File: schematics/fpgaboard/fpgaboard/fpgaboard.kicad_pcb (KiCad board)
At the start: 4 copper layers, 67.6 x 37.5 mm, 14 parts, among them J1 SODIMM-200, U1 LFE5UM-85F-8BG381I, U13 W25Q32JVSS, U2 AMS1117-3.3, U3 IS42S16320F-7TL, U4 IS42S16320F-7TL

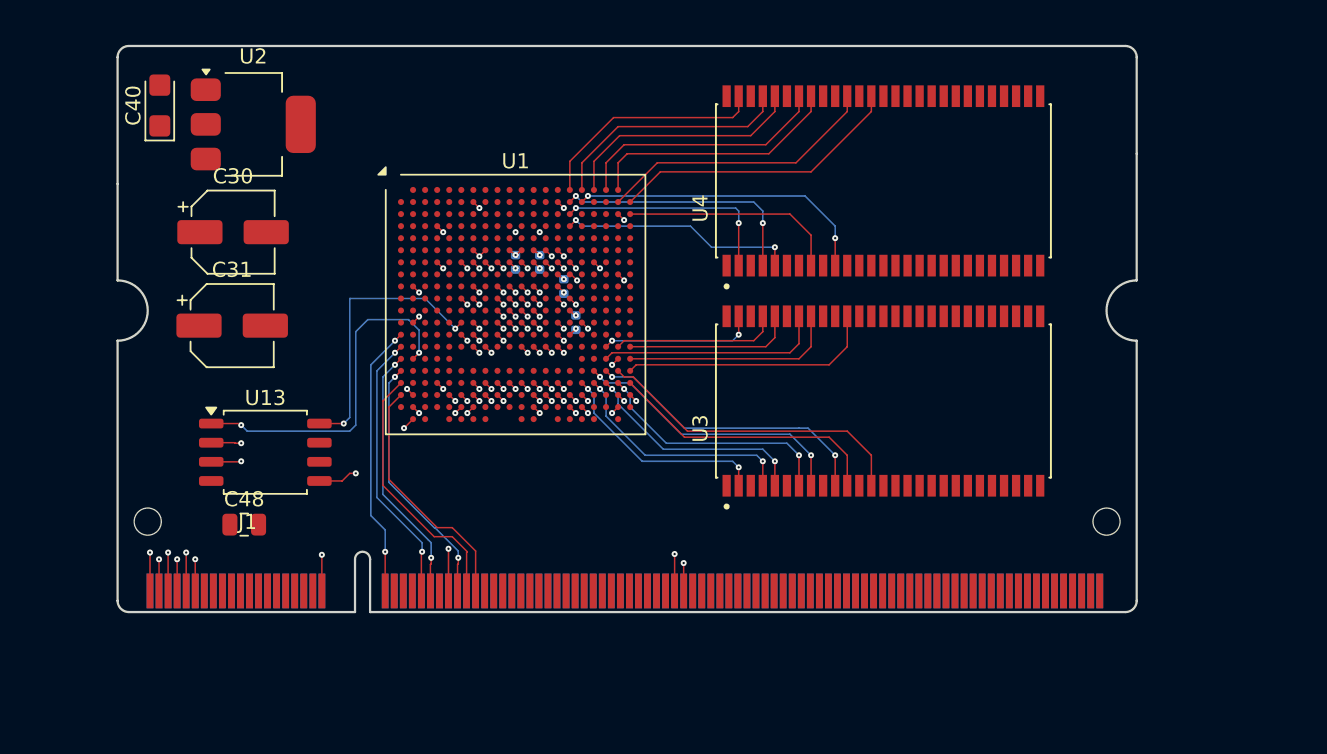
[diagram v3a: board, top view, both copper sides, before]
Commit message: FPGA board update; using 6 layer setup and "via in pad".
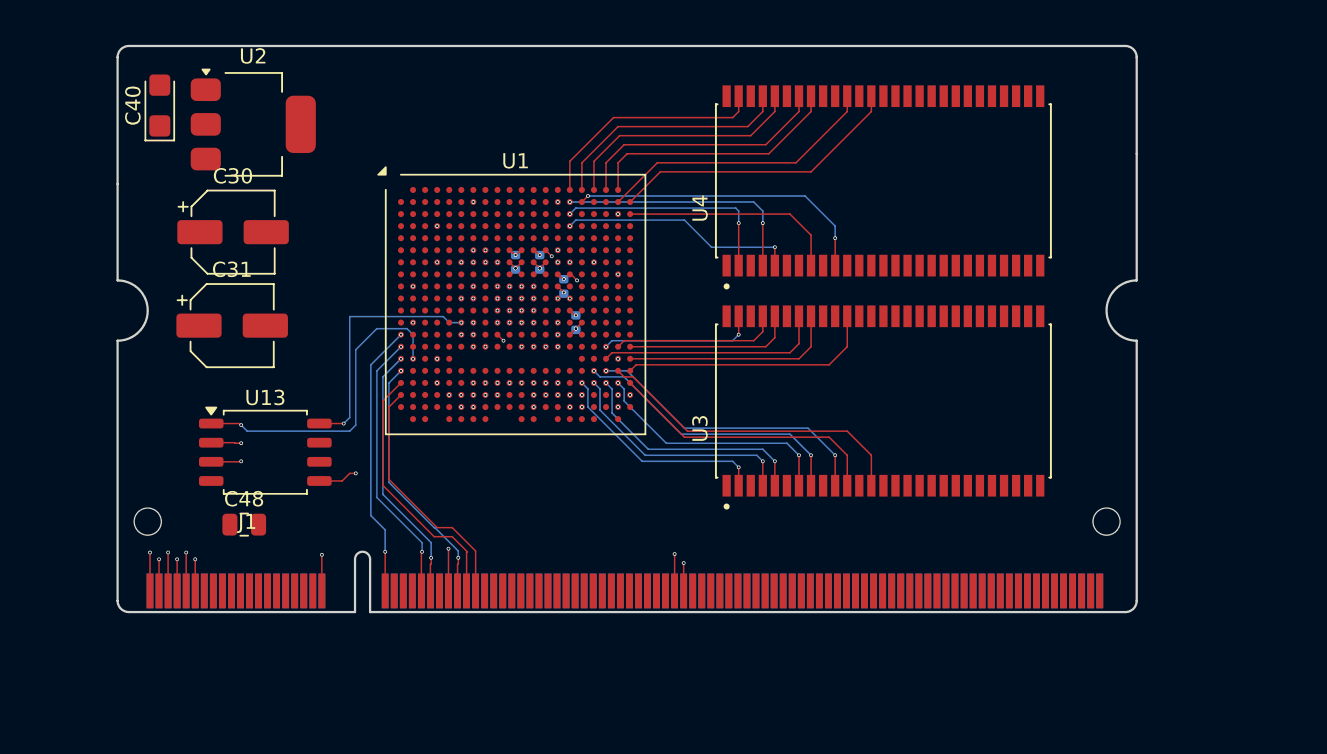
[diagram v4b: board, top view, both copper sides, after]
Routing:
- net GND: track 72.3 -> 28.0 mm
- net IO_3v3: track 21.8 -> 19.8 mm
- net FLASH_CSn: track 23.0 -> 21.1 mm
- net FLASH_IO2: track 2.85 -> 2.00 mm, vias 2 -> 1
- net RAM_D2: track 15.3 -> 15.9 mm
- net FLASH_IO1: track 2.57 -> 2.00 mm, vias 2 -> 1
- net FLASH_IO0: track 3.19 -> 2.62 mm, vias 2 -> 1
- added copper zone on In4.Cu, net IO_3v3
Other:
- copper layers 4 -> 6

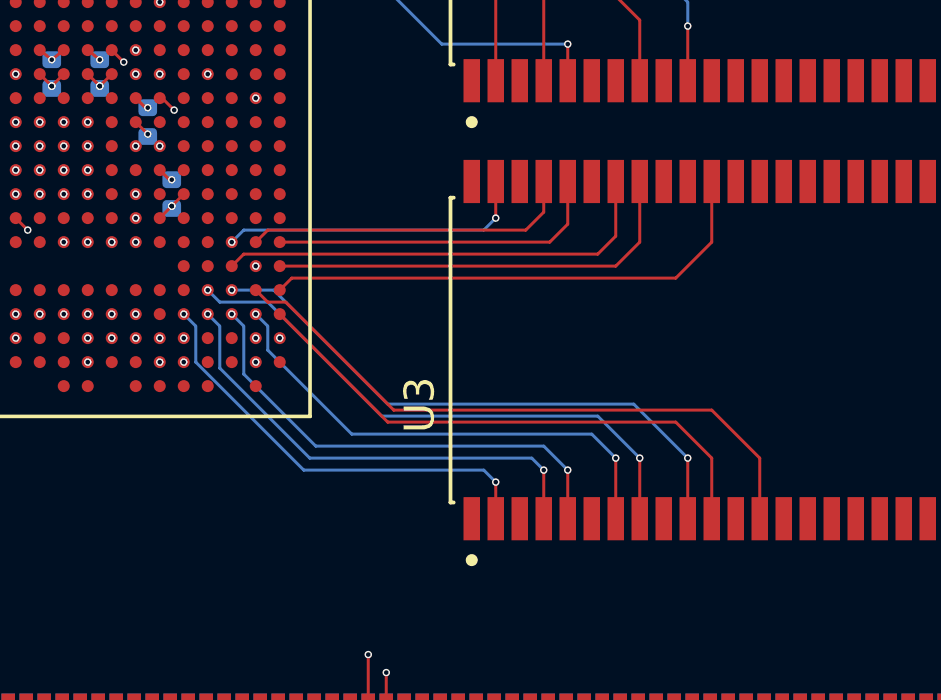
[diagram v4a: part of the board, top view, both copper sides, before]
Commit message: Rerouting some wires on FPGA board.
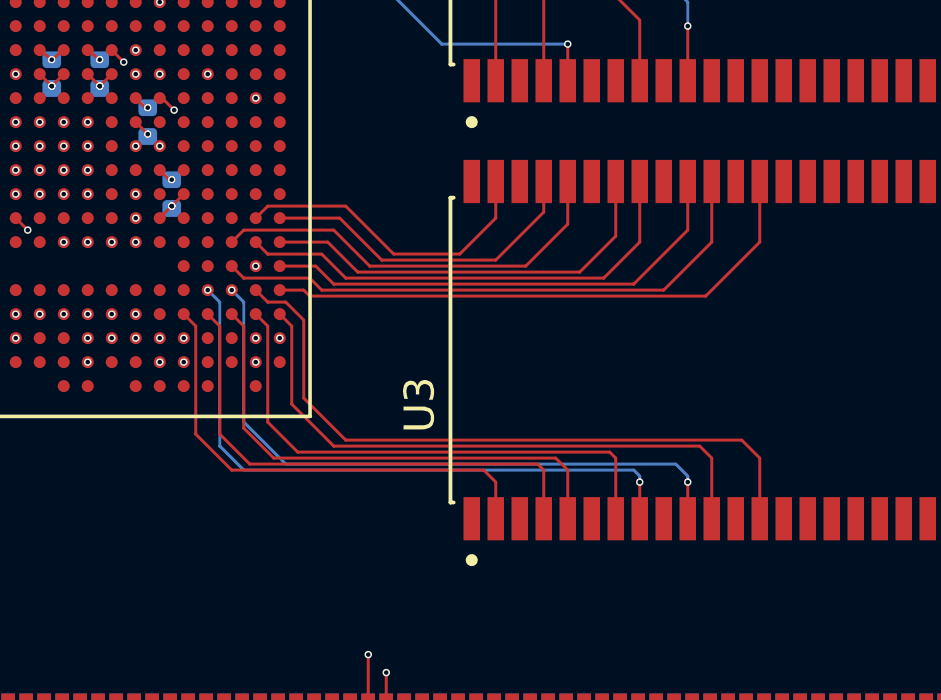
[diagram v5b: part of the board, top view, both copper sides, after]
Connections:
- U1 pad N19: RAM_D10 -> RAM_D15
- U1 pad N20: RAM_D8 -> RAM_D14
- U1 pad P18: RAM_D15 -> RAM_D13
- U1 pad P19: RAM_D14 -> RAM_D11
- U1 pad P20: RAM_D13 -> RAM_D12
- U1 pad R18: RAM_D12 -> RAM_D9
- U1 pad R20: RAM_D11 -> RAM_D10
- U1 pad T20: RAM_D9 -> RAM_D8
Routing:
- net RAM_D8: track 0.00 -> 18.8 mm
- net RAM_D10: track 0.00 -> 16.2 mm
- net RAM_D13: track 11.3 -> 13.9 mm
- net RAM_D4: track 18.7 -> 21.2 mm
- net RAM_D5: track 19.5 -> 21.5 mm
- net RAM_D9: track 17.1 -> 19.0 mm
- net RAM_D6: track 18.4 -> 19.9 mm
- net RAM_D7: track 21.1 -> 22.7 mm
- net RAM_D11: track 14.4 -> 15.8 mm
- net RAM_D3: track 16.5 -> 17.9 mm, vias 2 -> 0
- net RAM_D0: track 14.6 -> 16.0 mm, vias 2 -> 0
- net RAM_D1: track 15.8 -> 17.1 mm, vias 2 -> 0
- net RAM_D12: track 15.0 -> 13.9 mm
- net RAM_D2: track 15.9 -> 17.0 mm, vias 2 -> 0
- net RAM_D15: track 10.4 -> 10.5 mm, vias 2 -> 0

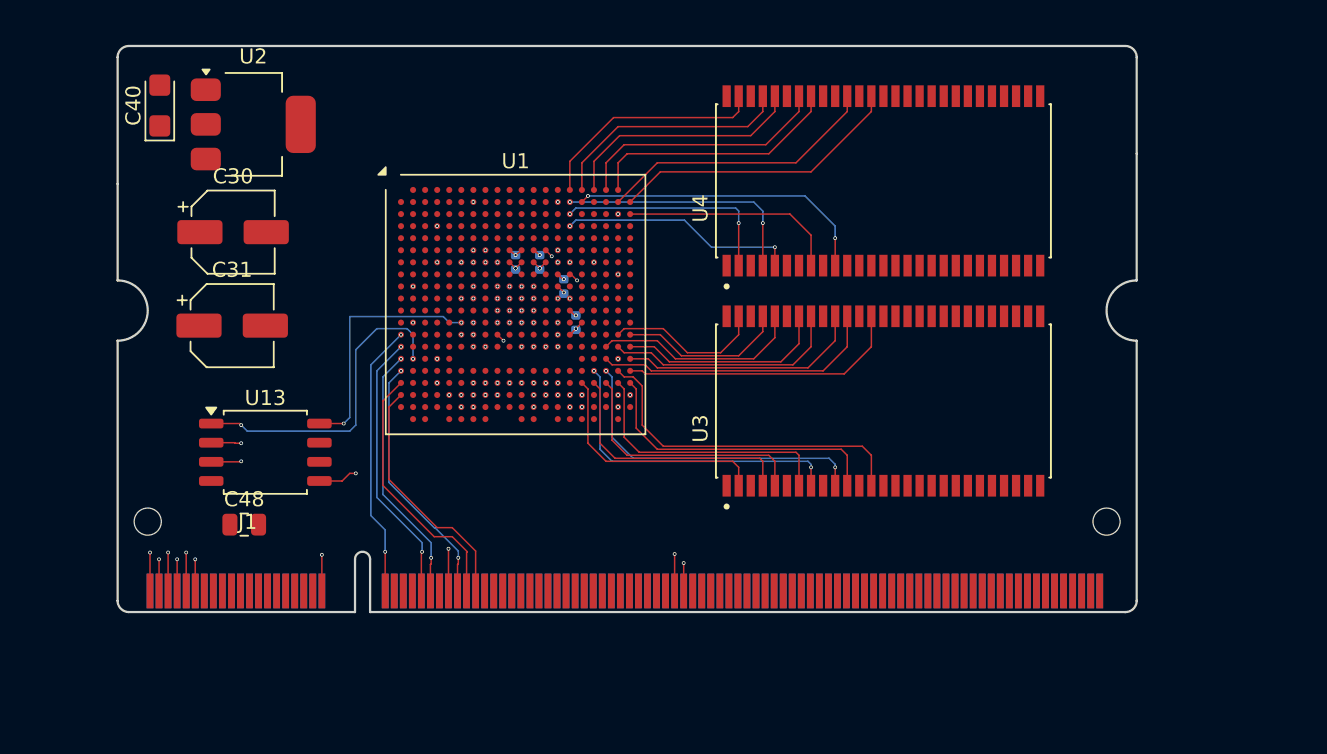
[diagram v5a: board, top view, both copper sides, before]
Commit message: More work on FPGA board.
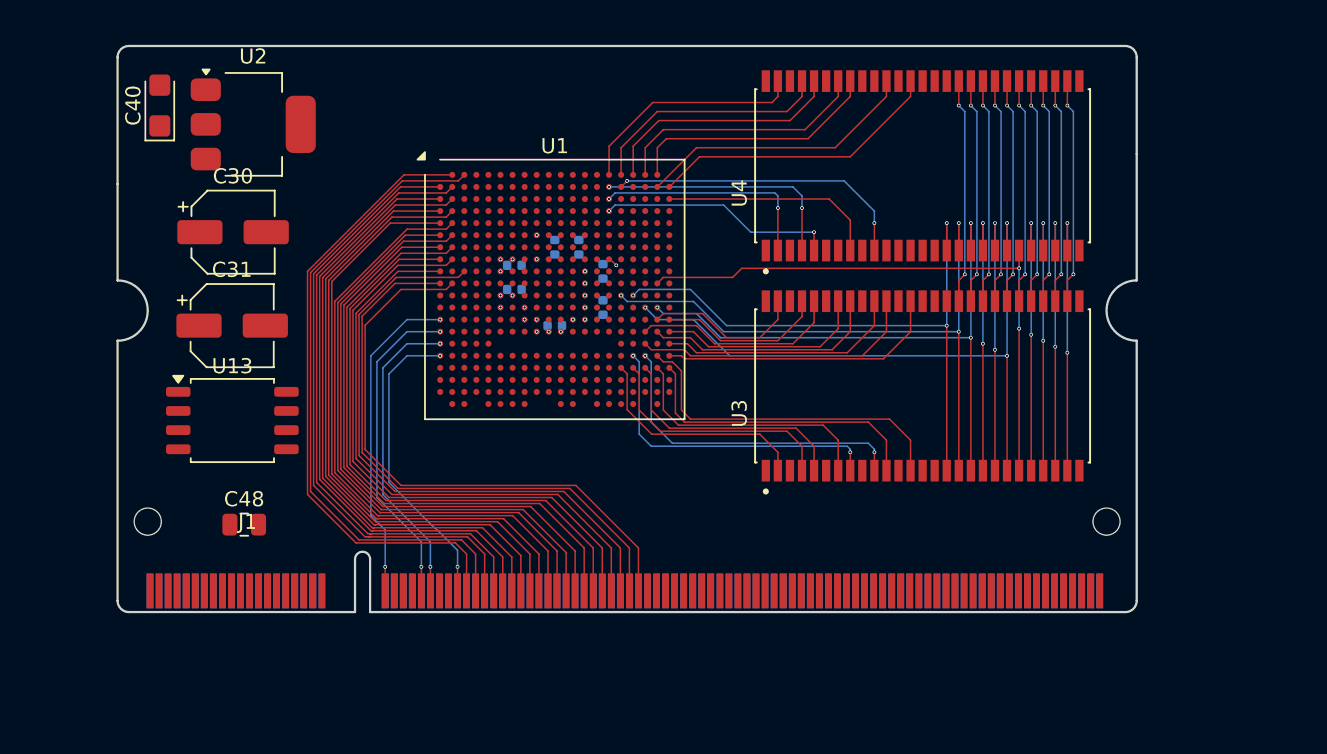
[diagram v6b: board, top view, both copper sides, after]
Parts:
- added C5: C_Small, Capacitor_SMD:C_0402_1005Metric, B.Cu at (146.1, 76.2)
- added C6: C_Small, Capacitor_SMD:C_0402_1005Metric, B.Cu at (146.1, 74.6)
- added C7: C_Small, Capacitor_SMD:C_0402_1005Metric, B.Cu at (148.8, 78.6)
- moved U13 3.04 mm to (127.4, 84.9)
- moved C1 2.79 mm to (148.8, 73.4)
- moved U1 2.79 mm to (148.8, 76.2)
- moved C2 2.79 mm to (150.4, 73.4)
- moved C3 2.79 mm to (152.0, 75.0)
- moved U3 2.79 mm to (173.2, 82.6)
- moved U4 2.79 mm to (173.2, 68.0)
- moved C4 2.06 mm to (152.0, 77.4)
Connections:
- U1 pad A2: unconnected-(U1G-PL35A-PadA2) -> S5
- U1 pad A3: unconnected-(U1G-PL14C-PadA3) -> S6
- U1 pad B1: unconnected-(U1G-PL35B-PadB1) -> S7
- U1 pad B2: unconnected-(U1G-PL35C-PadB2) -> S8
- U1 pad C1: unconnected-(U1G-PL38A-PadC1) -> S9
- U1 pad C2: unconnected-(U1G-PL35D-PadC2) -> S10
- U1 pad D1: unconnected-(U1G-PL38B-PadD1) -> S11
- U1 pad D2: unconnected-(U1G-PL38C-PadD2) -> S12
- U1 pad E1: unconnected-(U1G-PL38D-PadE1) -> S13
- U1 pad E2: unconnected-(U1G-PL44D-PadE2) -> S14
- U1 pad F1: unconnected-(U1F-PL47B-PadF1) -> S15
- U1 pad F2: unconnected-(U1G-PL44C-PadF2) -> S16
- U1 pad G1: unconnected-(U1F-PL47D-PadG1) -> S17
- U1 pad G2: unconnected-(U1F-PL47A-PadG2) -> S18
- U1 pad H1: unconnected-(U1F-PL53C-PadH1) -> S19
- U1 pad H2: unconnected-(U1F-PL47C-PadH2) -> S20
- U1 pad J1: unconnected-(U1F-PL53B-PadJ1) -> S21
- U1 pad J3: unconnected-(U1F-PL50C-PadJ3) -> S22
- U1 pad K1: unconnected-(U1F-PL53D-PadK1) -> S23
- U1 pad K2: unconnected-(U1F-PL53A-PadK2) -> S24
- U1 pad L18: unconnected-(U1E-PR50C-PadL18) -> RAM_BA0
- U1 pad M18: unconnected-(U1E-PR50D-PadM18) -> RAM_BA1
- U1 pad U1: S5 -> unconnected-(U1H-PB6A-PadU1)
- U1 pad V1: S6 -> unconnected-(U1H-PB6B-PadV1)
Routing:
- net RAM_BA1: track 0.00 -> 43.6 mm, vias 0 -> 3
- net ~{RAM_CAS}: track 0.00 -> 41.6 mm, vias 0 -> 3
- net S8: track 0.00 -> 41.2 mm
- net S10: track 0.00 -> 41.0 mm
- net S12: track 0.00 -> 41.0 mm
- net S7: track 0.00 -> 40.5 mm
- net S14: track 0.00 -> 40.2 mm
- net S22: track 0.00 -> 40.2 mm
- net ~{RAM_WE}: track 0.00 -> 40.2 mm, vias 0 -> 3
- net S9: track 0.00 -> 40.1 mm
- net S11: track 0.00 -> 40.0 mm
- net S16: track 0.00 -> 40.0 mm
- net S18: track 0.00 -> 40.0 mm
- net S13: track 0.00 -> 40.0 mm
- net ~{RAM_RAS}: track 0.00 -> 39.9 mm, vias 0 -> 3
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- added copper zone on In1.Cu, net IO_3v3
- removed copper zone on In1.Cu, net GND

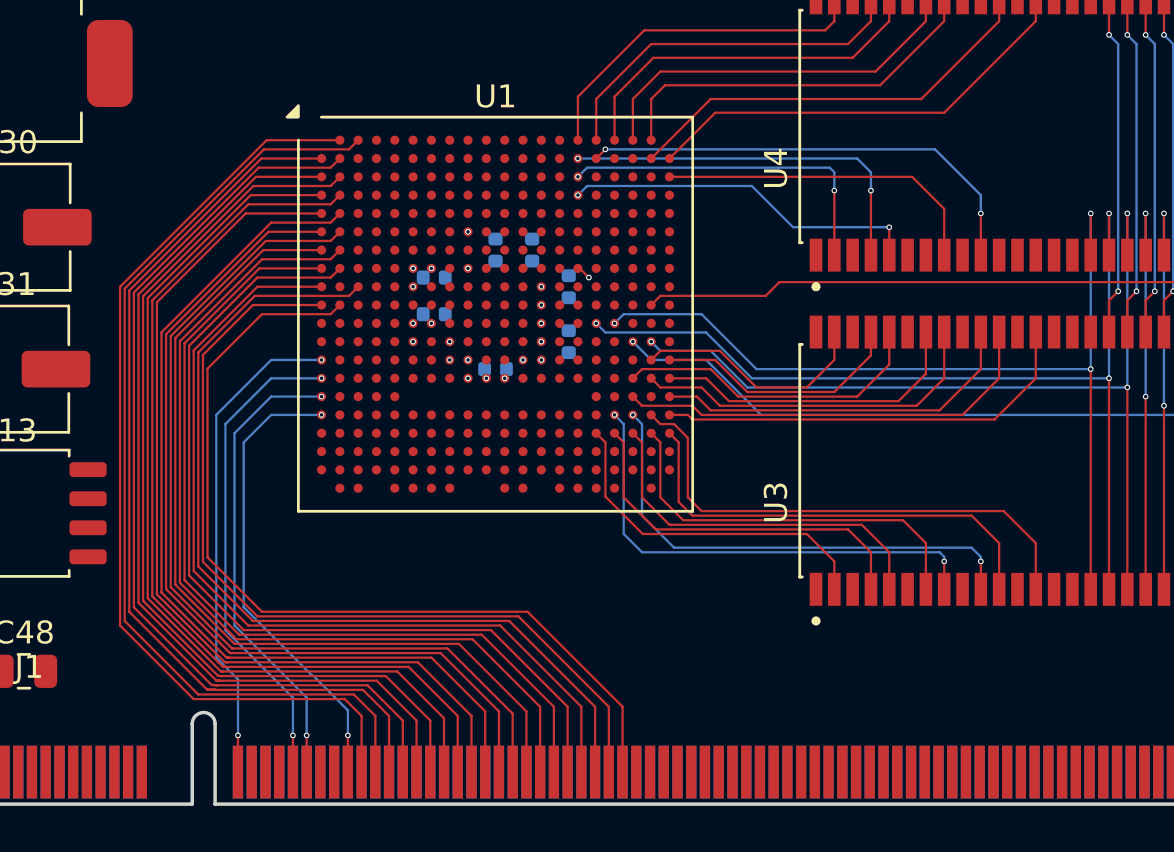
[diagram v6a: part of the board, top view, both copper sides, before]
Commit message: Top row of SODIMM wired up to FPGA in fpga board.
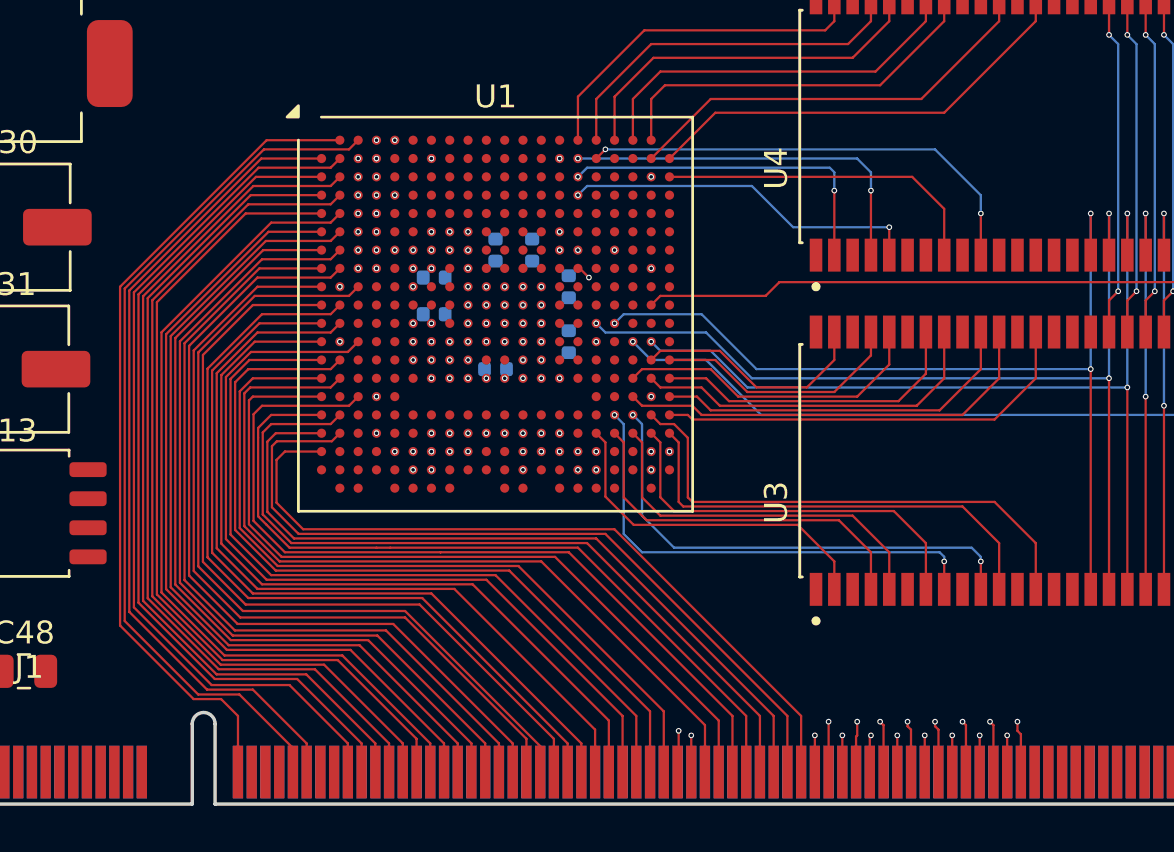
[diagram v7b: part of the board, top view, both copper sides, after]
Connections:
- U1 pad A2: S5 -> S1
- U1 pad A3: S6 -> S2
- U1 pad A4: unconnected-(U1G-PL11A-PadA4) -> S36
- U1 pad A5: unconnected-(U1G-PL11B-PadA5) -> S37
- U1 pad B1: S7 -> S3
- U1 pad B2: S8 -> S4
- U1 pad B3: unconnected-(U1G-PL14D-PadB3) -> S38
- U1 pad B4: unconnected-(U1G-PL14B-PadB4) -> S39
- U1 pad C1: S9 -> S5
- U1 pad C2: S10 -> S6
- U1 pad C3: unconnected-(U1G-PL17C-PadC3) -> S40
- U1 pad C4: unconnected-(U1G-PL14A-PadC4) -> S41
- U1 pad D1: S11 -> S7
- U1 pad D2: S12 -> S8
- U1 pad D3: unconnected-(U1G-PL17D-PadD3) -> S42
- U1 pad D5: unconnected-(U1G-PL17B-PadD5) -> S43
- U1 pad E1: S13 -> S9
- U1 pad E2: S14 -> S10
- U1 pad E3: unconnected-(U1G-PL20B-PadE3) -> S44
- U1 pad E4: unconnected-(U1G-PL17A-PadE4) -> S45
- U1 pad F1: S15 -> S11
- U1 pad F2: S16 -> S12
- U1 pad F3: unconnected-(U1G-PL44B-PadF3) -> S46
- U1 pad F4: unconnected-(U1G-PL20A-PadF4) -> S47
- U1 pad G1: S17 -> S13
- U1 pad G2: S18 -> S14
- U1 pad G3: unconnected-(U1G-PL44A-PadG3) -> S48
- U1 pad G5: unconnected-(U1G-PL41B-PadG5) -> S49
- U1 pad H1: S19 -> S15
- U1 pad H2: S20 -> S16
- U1 pad H3: unconnected-(U1G-PL41D-PadH3) -> S50
- U1 pad H4: unconnected-(U1G-PL41A-PadH4) -> S51
- U1 pad J1: S21 -> S17
- U1 pad J3: S22 -> S18
- U1 pad K1: S23 -> S19
- U1 pad K2: S24 -> S20
- U1 pad L1: unconnected-(U1F-PL89C-PadL1) -> S21
- U1 pad L2: unconnected-(U1F-PL86D-PadL2) -> S22
- U1 pad M1: unconnected-(U1F-PL89B-PadM1) -> S23
- U1 pad M3: unconnected-(U1F-PL86B-PadM3) -> S24
- U1 pad N1: S1 -> S25
- U1 pad N2: unconnected-(U1F-PL89A-PadN2) -> S26
- U1 pad P1: S2 -> S27
- U1 pad P2: unconnected-(U1F-PL92B-PadP2) -> S28
- U1 pad R1: S3 -> S29
- U1 pad R3: unconnected-(U1H-PB15B-PadR3) -> S30
- U1 pad T1: S4 -> S31
- U1 pad T2: unconnected-(U1H-PB13A-PadT2) -> S32
- U1 pad U1: unconnected-(U1H-PB6A-PadU1) -> S33
- U1 pad U2: unconnected-(U1H-PB13B-PadU2) -> S34
- U1 pad V1: unconnected-(U1H-PB6B-PadV1) -> S35
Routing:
- net S37: track 0.00 -> 61.4 mm, vias 0 -> 2
- net S36: track 0.00 -> 60.4 mm, vias 0 -> 2
- net S39: track 0.00 -> 60.4 mm, vias 0 -> 2
- net S43: track 0.00 -> 60.3 mm, vias 0 -> 2
- net S41: track 0.00 -> 59.9 mm, vias 0 -> 2
- net S38: track 0.00 -> 59.5 mm, vias 0 -> 2
- net S40: track 0.00 -> 59.2 mm, vias 0 -> 2
- net S45: track 0.00 -> 59.1 mm, vias 0 -> 2
- net S49: track 0.00 -> 59.1 mm, vias 0 -> 2
- net S42: track 0.00 -> 58.8 mm, vias 0 -> 2
- net S47: track 0.00 -> 58.7 mm, vias 0 -> 2
- net S44: track 0.00 -> 58.4 mm, vias 0 -> 2
- net S46: track 0.00 -> 58.0 mm, vias 0 -> 2
- net S51: track 0.00 -> 57.9 mm, vias 0 -> 2
- net S48: track 0.00 -> 57.6 mm, vias 0 -> 2
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- added copper zone on In1.Cu, net GND
- removed copper zone on In1.Cu, net IO_3v3

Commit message: Begun working on FPGA board SODIMM bottom routing.
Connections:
- U1 pad A11: unconnected-(U1B-PT63B-PadA11) -> S56
- U1 pad A12: unconnected-(U1C-PT76A-PadA12) -> S54
- U1 pad A13: unconnected-(U1C-PT76B-PadA13) -> S52
- U1 pad B11: unconnected-(U1B-PT65A-PadB11) -> S57
- U1 pad B12: unconnected-(U1C-PT71A-PadB12) -> S55
- U1 pad B13: unconnected-(U1C-PT78A-PadB13) -> S53
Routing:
- net S53: track 0.00 -> 54.0 mm, vias 0 -> 1
- net S52: track 0.00 -> 53.7 mm, vias 0 -> 1
- net S55: track 0.00 -> 52.3 mm, vias 0 -> 1
- net S54: track 0.00 -> 52.1 mm, vias 0 -> 1
- net S56: track 0.00 -> 50.8 mm, vias 0 -> 1
- net S57: track 0.00 -> 50.6 mm, vias 0 -> 1
